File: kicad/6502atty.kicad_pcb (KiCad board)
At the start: 2 copper layers, 104.9 x 108.3 mm, 104 parts, among them J1 Conn_01x04_Pin, J10 Conn_01x04_Pin, J11 Conn_01x03_Pin, J12 Conn_01x02_Pin, J2 Conn_01x02_Pin, J3 Conn_02x03_Odd_Even, J4 Conn_01x03_Pin, J5 Conn_01x06_Pin, J6 Conn_01x04_Pin, J7 Conn_01x10_Pin, J8 Conn_01x03_Pin, J9 Conn_01x10_Pin, SW1 SW_Push, U1 ATmega164P-20P, U10 74LS08, U11 74LS138, U12 74LS574, U2 74LS112, U3 W65C02SxP, U4 74LS574, U5 74HC245, U6 27C128, U7 KM62256CLP, U8 74LS00, U9 74LS00, Y1 18.432MHz

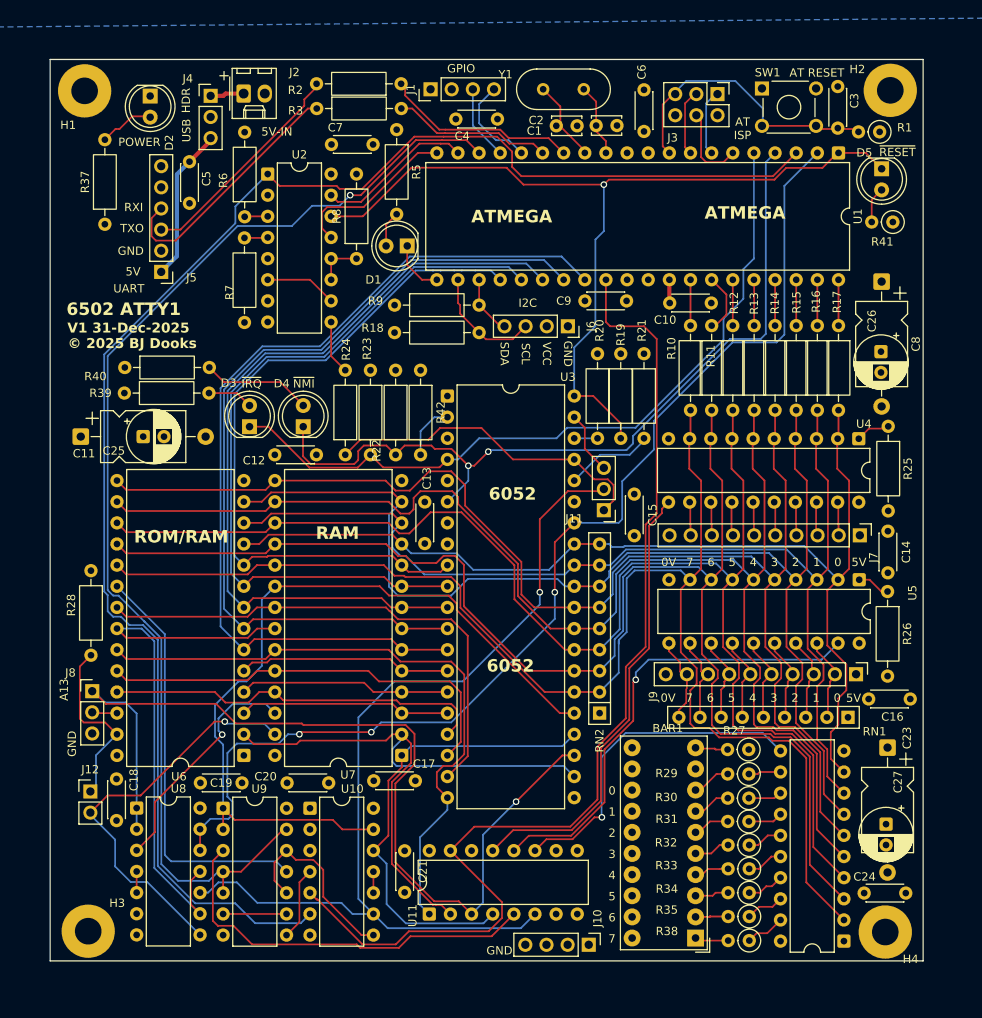
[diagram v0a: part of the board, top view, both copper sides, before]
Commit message: pcb: move around stuff to make pcb smaller
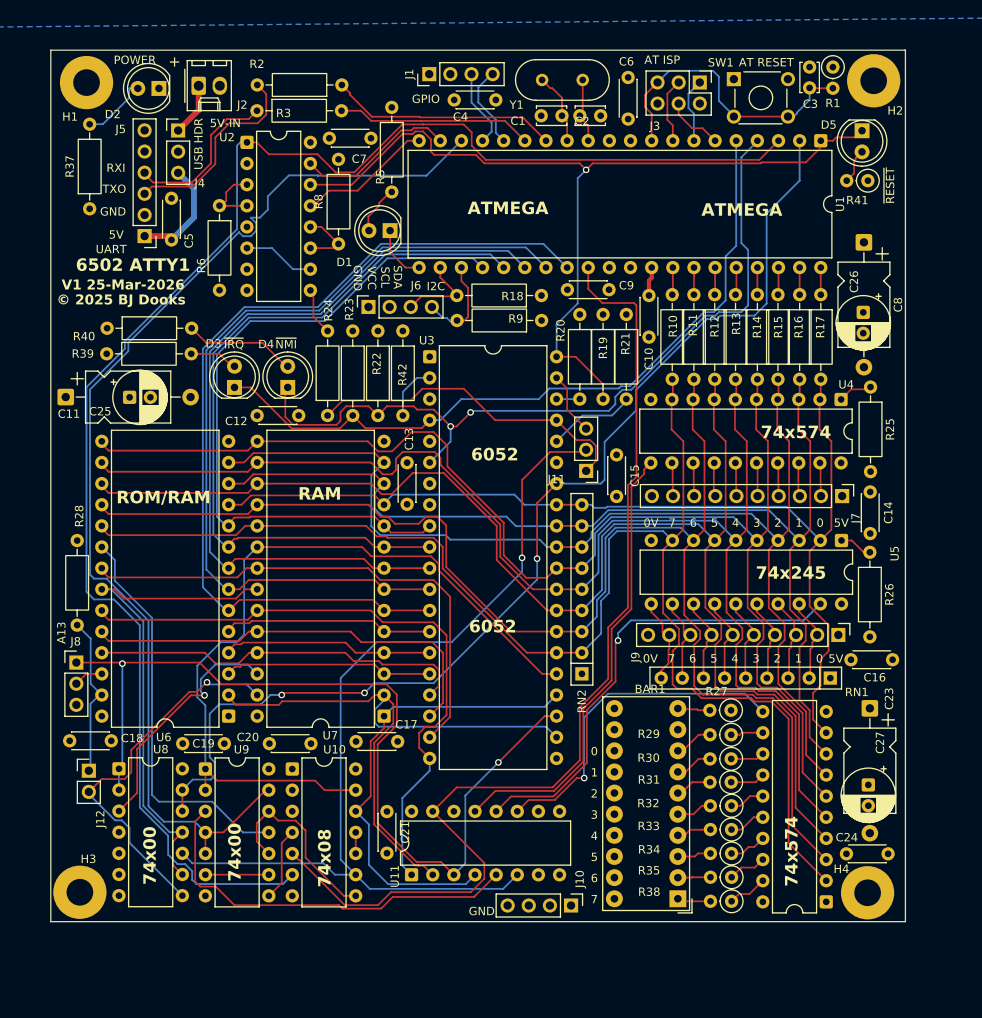
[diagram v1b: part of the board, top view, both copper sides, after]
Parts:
- removed R7: 4K7, Resistor_THT:R_Axial_DIN0207_L6.3mm_D2.5mm_P10.16mm_Horizontal
- C3: value ~ -> ?; footprint Capacitor_THT:C_Disc_D4.3mm_W1.9mm_P5.00mm -> Capacitor_THT:C_Disc_D3.4mm_W2.1mm_P2.50mm
- moved J6 24.1 mm to (38.2, 31.0), turned to 90 degrees
- moved R18 18.2 mm to (59.0, 29.6), turned to 180 degrees
- moved R9 17.8 mm to (59.0, 32.6), turned to 180 degrees
- moved C5 9.64 mm to (14.5, 22.9), turned to 90 degrees
- moved R1 9.60 mm to (94.0, 2.14), turned to -90 degrees
- moved R3 7.19 mm to (24.8, 7.38)
- moved R2 7.12 mm to (35.0, 4.28)
- moved C3 5.90 mm to (91.2, 4.63)
- moved R41 5.81 mm to (98.2, 15.8)
- moved J4 5.71 mm to (15.3, 9.76)
- moved J2 5.48 mm to (17.8, 4.38)
- moved C23 5.17 mm to (98.4, 79.2)
- moved U8 5.17 mm to (8.19, 86.4)
- moved U11 5.17 mm to (43.4, 99.2)
- moved U12 5.17 mm to (93.2, 102.4)
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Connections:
- U2 pad 4: Net-(U2A-~{S}) -> Net-(U2A-J)
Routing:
- net /Atmel Controller/U_RXI: track 30.5 -> 19.6 mm
- net /ROM_SEL: track 141.7 -> 135.7 mm, vias 1 -> 0
- net /~{R}W: track 66.9 -> 61.2 mm
- net /A13: track 115.0 -> 109.4 mm, vias 1 -> 2
- net Net-(U2A-J): track 2.79 -> 8.24 mm
- net /SDA: track 7.15 -> 12.5 mm
- net /Atmel Controller/U_5V: track 18.5 -> 13.4 mm
- net /Atmel Controller/AT_D6: track 7.44 -> 2.73 mm
- net /Atmel Controller/TXD0: track 19.2 -> 23.5 mm
- net /PWM_CLK: track 20.2 -> 16.3 mm
- net /Atmel Controller/RXD0: track 23.5 -> 27.4 mm
- net /AT_~{CE}: track 128.1 -> 124.5 mm
- net /D2: track 138.0 -> 134.6 mm
- net /SCL: track 14.0 -> 10.5 mm
- net /Atmel Controller/AT_D7: track 5.97 -> 2.72 mm
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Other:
- board size 104.9 x 108.3 mm -> 102.7 x 104.7 mm
- board text added: "74x00"
- board text added: "74x08"
- board text added: "74x245"
- board text added: "74x574"
- board text added: "V1 25-Mar-2026"
- board text removed: "V1 31-Dec-2025"

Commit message: pcb: run production output
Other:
- board text added: "74x138"
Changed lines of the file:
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@@
+		)
+	)
+	(gr_text "74x138"
+		(at 52.5 96.3 0)
+		(layer "F.SilkS")
+		(effects
+			(font
+				(size 1.5 1.5)
+				(thickness 0.3)
+				(bold yes)
+			)
+			(justify left bottom)
 		)
 	)

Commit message: pcb: minor schematic updates
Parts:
- R24: value 1K -> 560R
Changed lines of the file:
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@@
 			)
 		)
-		(property "Value" "1K"
+		(property "Value" "560R"
 			(at 5.08 2.37 90)
 			(layer "F.Fab")

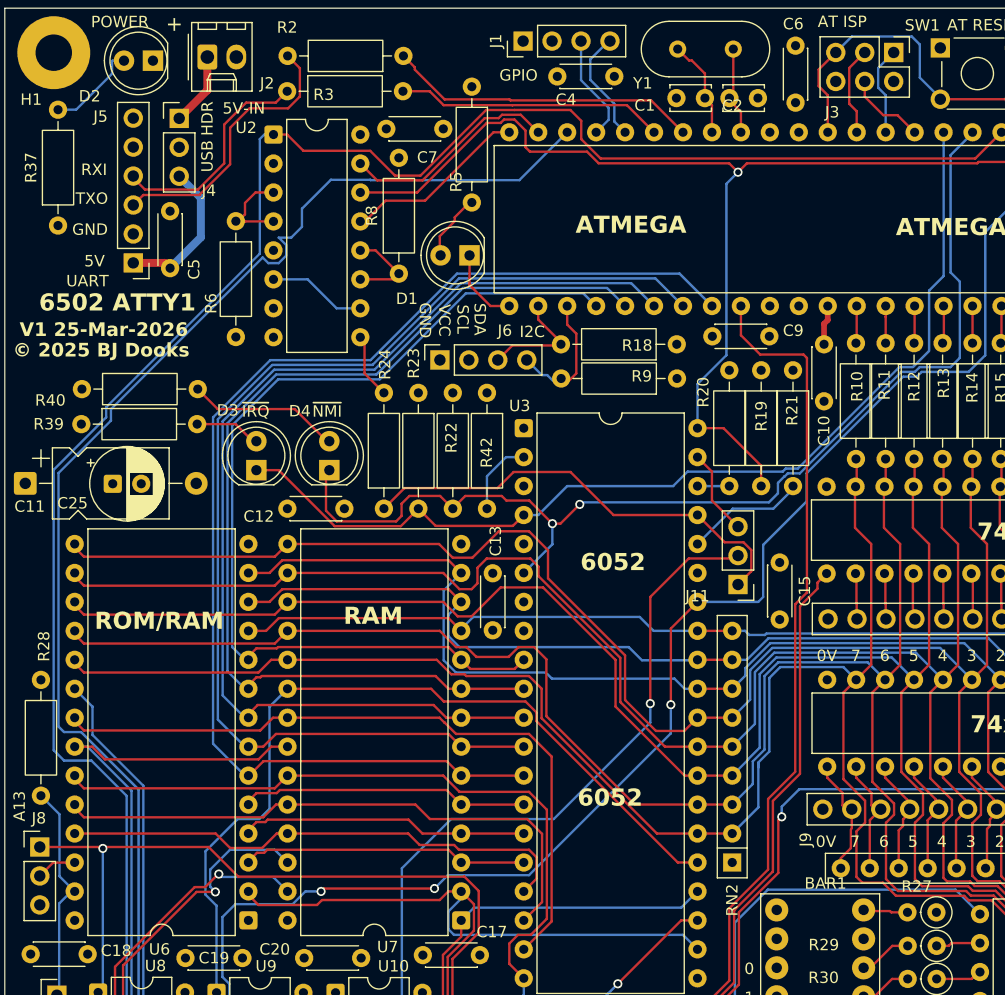
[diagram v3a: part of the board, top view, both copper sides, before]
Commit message: pcb: minor routing fixes, add rjek's bee
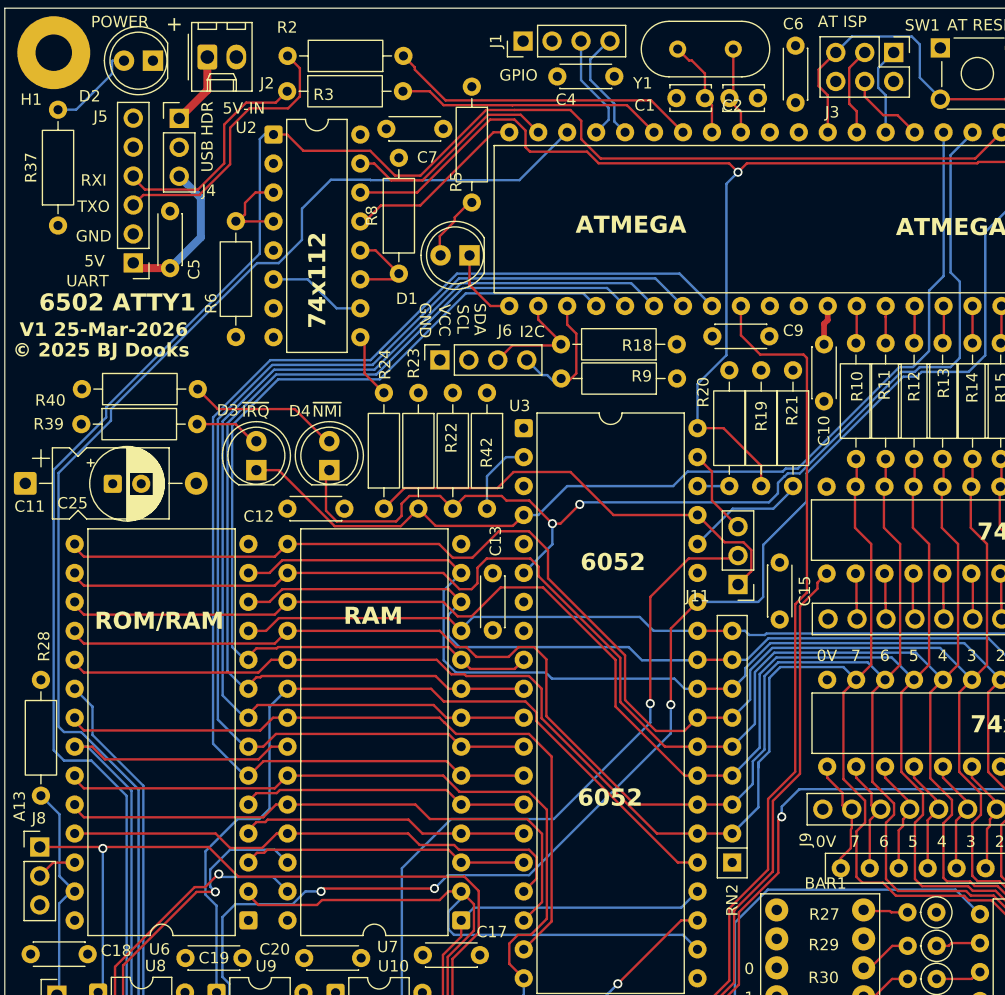
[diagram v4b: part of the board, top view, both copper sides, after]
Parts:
- added REF**: Untitled, rjek:rjek bee, B.Cu at (87.5, 18.7)
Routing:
- net /ROM_SEL: track 135.7 -> 134.1 mm
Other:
- board text added: "74x112"

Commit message: pcb: silkscreen updates, minor routing updates
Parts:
- moved H4 0.65 mm to (98.7, 101.0)
- moved J1 0.62 mm to (45.5, 3.60)
- moved C27 0.59 mm to (98.4, 87.8)
- moved C4 0.52 mm to (48.5, 6.60)
- moved H1 0.51 mm to (3.80, 3.90)
- moved C23 0.28 mm to (98.4, 78.9)
- moved C24 0.25 mm to (95.8, 96.5)
- moved H2 0.23 mm to (99.1, 3.80)
- moved H3 0.21 mm to (3.60, 101.1)
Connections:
- U10 pad 4: /control/~{AT_ROM} -> /AT_~{CE}
- U10 pad 5: /AT_~{CE} -> /control/~{AT_ROM}
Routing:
- net /AT_~{CE}: track 124.5 -> 120.9 mm
- net /control/ROM_ACC: track 22.9 -> 19.8 mm
- net /control/~{AT_ROM}: track 8.79 -> 6.25 mm
- net /Atmel Controller/~{AT_RESET}: track 36.1 -> 36.9 mm
- net /R~{W}ph: track 45.8 -> 45.2 mm
- net /Atmel Controller/PD3: track 9.46 -> 8.85 mm
- net /Atmel Controller/PD2: track 10.0 -> 9.44 mm
- net /~{A13}: track 29.2 -> 28.7 mm
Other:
- board text added: "D2"
- board text added: "D3"
- board text added: "P2o"

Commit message: v1_r2 production data
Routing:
- net /Atmel Controller/U_5V: track 13.4 -> 12.6 mm
